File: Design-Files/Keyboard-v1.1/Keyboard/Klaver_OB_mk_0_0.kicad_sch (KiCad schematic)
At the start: 322 parts, among them J1 TYPE-C-31-M-13C, J3 Conn_01x04, J4 Conn_01x03, J5 TYPE-C-31-M-13C, J7 Conn_01x04, J8 Conn_01x03, Q1 BSS138, Q2 BSS138, U1 RP2040, U2 NCP1117LPST33T3G, U3 TPD4E05U06DQAR, U4 W25Q128JVSIQ, U5 TPD4E05U06DQAR, U6 W25Q128JVSIQ, U7 NCP1117LPST33T3G, U8 RP2040, Y1 12MHz 18pF, Y2 12MHz 18pF

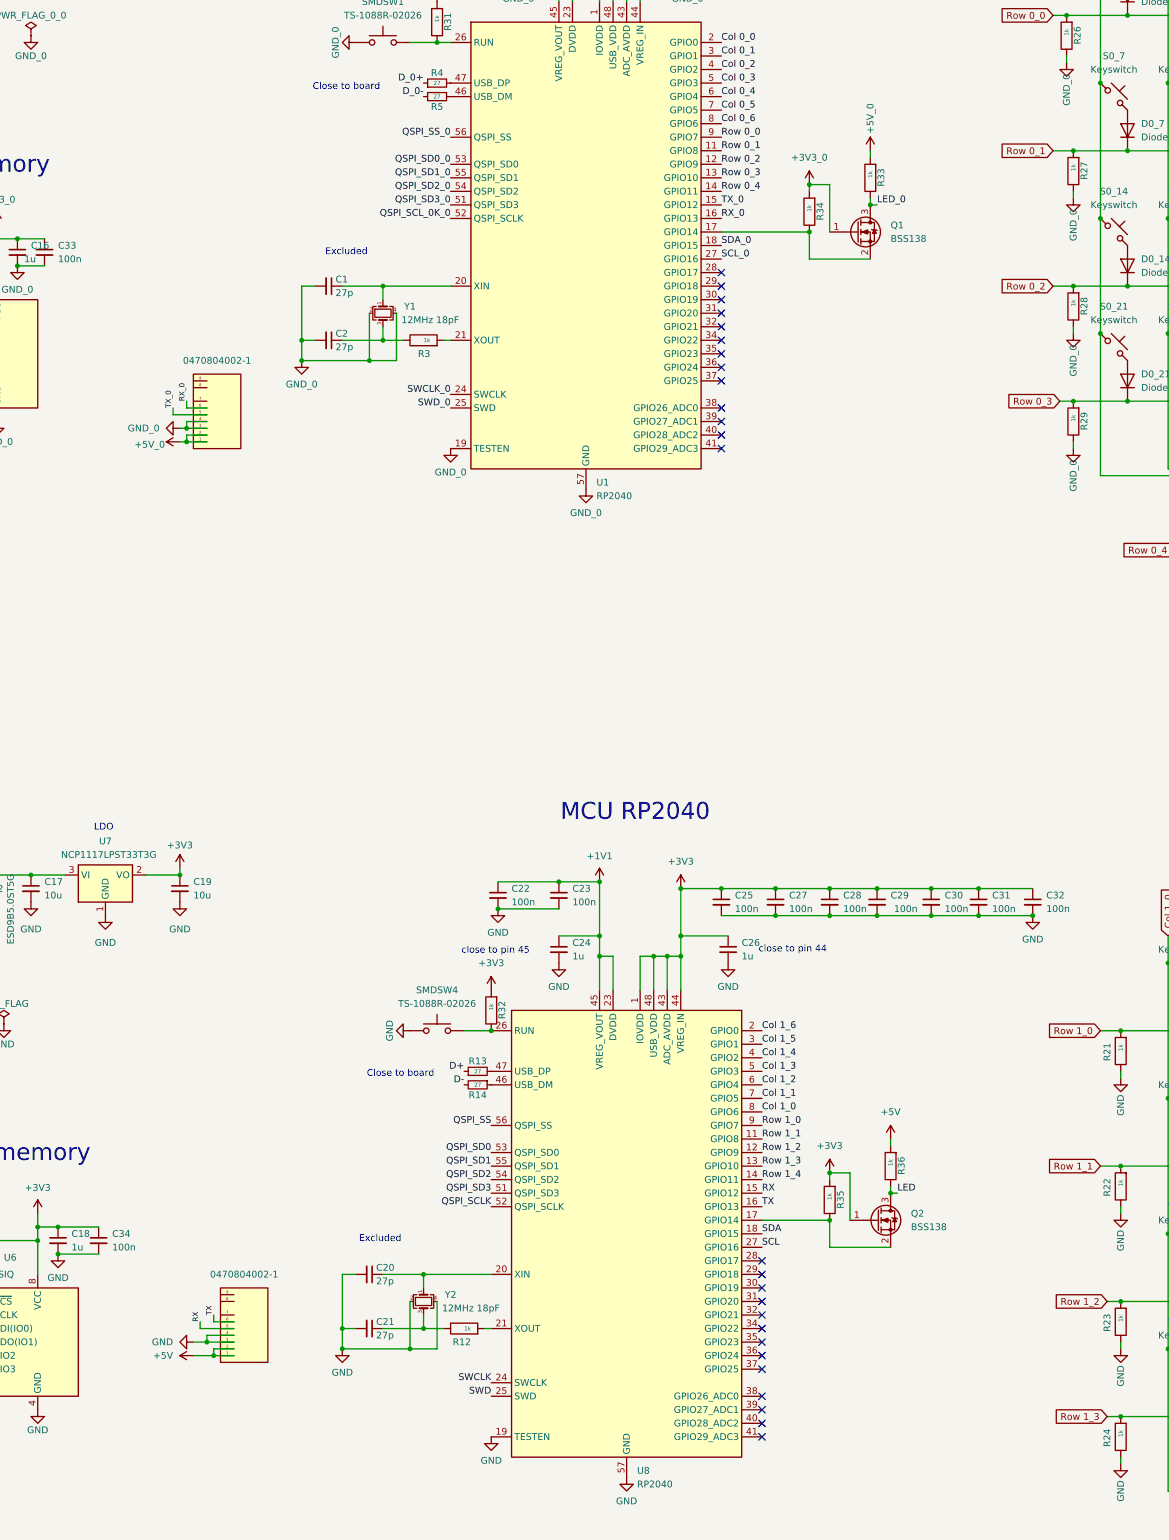
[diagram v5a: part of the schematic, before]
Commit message: #3  changed trrs connector and added zener diodes
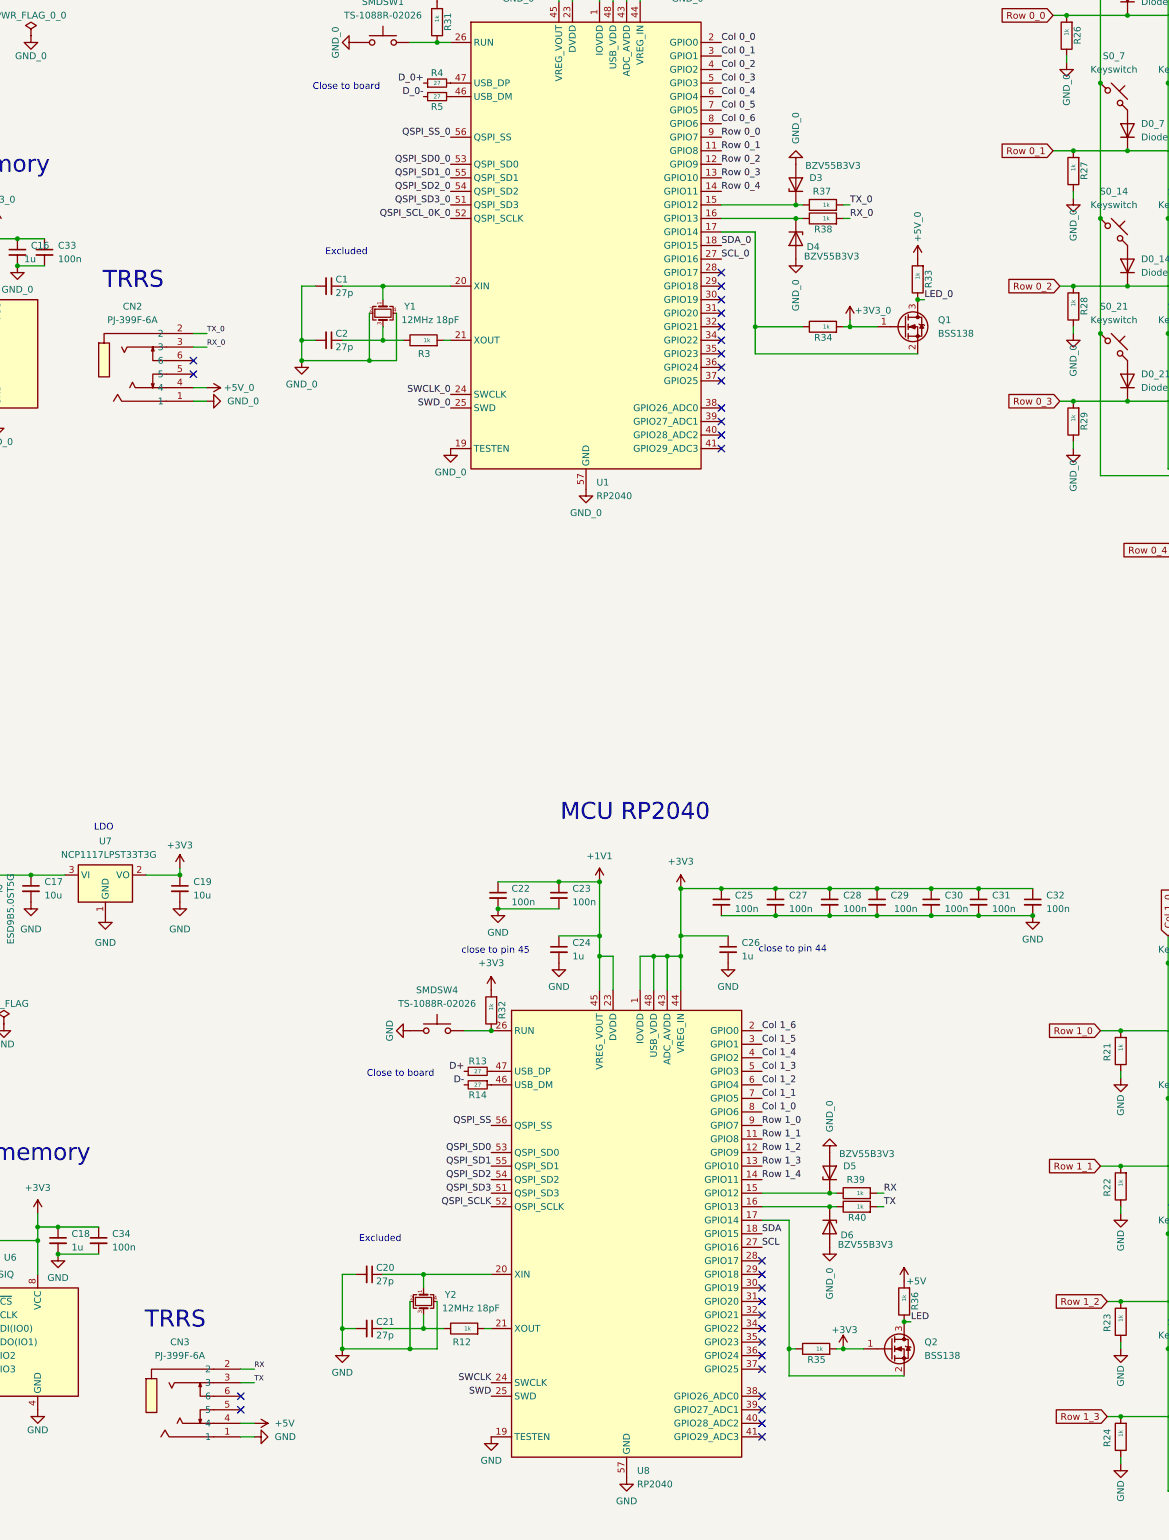
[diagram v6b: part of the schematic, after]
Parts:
- removed sata1, sata3: 0470804002-1, sata molex 2:sata molex1, symbol 5607-4200-SH:0470804002new
- added CN2, CN3: PJ-399F-6A, easyeda2kicad:AUDIO-SMD_PJ-399F-6A, symbol Library:PJ-399F-6A
- added D3, D4, D5, D6: BZV55B3V3, Diode_SMD:D_MiniMELF, symbol Diode:BZV55B3V3
- added R37, R38, R39, R40: 1k, Resistor_SMD:R_0402_1005Metric, symbol Library:R
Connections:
- net +5V: now also CN3.4
- net +5V_0: now also CN2.4
- net GND: now also CN3.1
- net GND_0: now also CN2.1, D3.2 (A), D4.2 (A), D5.2 (A), D6.2 (A)
- net RX: now also CN3.2, R39.2; no longer U8.15 (GPIO12)
- net RX_0: now also CN2.3, R38.2; no longer U1.16 (GPIO13)
- net TX: now also CN3.3, R40.2; no longer U8.16 (GPIO13)
- net TX_0: now also CN2.2, R37.2; no longer U1.15 (GPIO12)
- new net: D6.1 (K), R40.1, U8.16 (GPIO13)
- new net: D3.1 (K), R37.1, U1.15 (GPIO12)
- new net: D4.1 (K), R38.1, U1.16 (GPIO13)
- new net: D5.1 (K), R39.1, U8.15 (GPIO12)
- no-connect marks 32 -> 36
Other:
- note added: "TRRS"
- moved on the sheet: Q1, Q2, R33, R34, R35, R36

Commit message: #3 corrected TX RX
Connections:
- net RX: now also R40.2; no longer R39.2
- net TX: now also R39.2; no longer R40.2
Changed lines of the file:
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@@
 	(wire
 		(pts
+			(xy 273.05 281.94) (xy 274.32 281.94)
+		)
+		(stroke
+			(width 0)
+			(type default)
+		)
+	)
+	(wire
+		(pts
 			(xy 472.44 224.79) (xy 480.06 224.79)
 		)
@@
 	(wire
 		(pts
-			(xy 273.05 281.94) (xy 274.32 281.94)
-		)
-		(stroke
-			(width 0)
-			(type default)
-		)
-	)
-	(wire
-		(pts
 			(xy 201.93 226.06) (xy 213.36 226.06)
 		)
@@
 	(wire
 		(pts
-			(xy 273.05 279.4) (xy 274.32 279.4)
+			(xy 332.74 130.81) (xy 345.44 130.81)
 		)
 		(stroke
@@
 	(wire
 		(pts
-			(xy 332.74 130.81) (xy 345.44 130.81)
+			(xy 370.84 58.42) (xy 383.54 58.42)
 		)
 		(stroke
@@
 	(wire
 		(pts
-			(xy 370.84 58.42) (xy 383.54 58.42)
+			(xy 153.67 322.58) (xy 156.21 322.58)
 		)
 		(stroke
@@
 	(wire
 		(pts
-			(xy 153.67 322.58) (xy 156.21 322.58)
+			(xy 327.66 231.14) (xy 327.66 236.22)
 		)
 		(stroke
@@
 	(wire
 		(pts
-			(xy 327.66 231.14) (xy 327.66 236.22)
+			(xy 387.35 139.7) (xy 365.76 139.7)
 		)
 		(stroke
@@
 	(wire
 		(pts
-			(xy 387.35 139.7) (xy 365.76 139.7)
+			(xy 314.96 71.12) (xy 314.96 96.52)
 		)
 		(stroke
@@
 	(wire
 		(pts
-			(xy 314.96 71.12) (xy 314.96 96.52)
+			(xy 538.48 227.33) (xy 538.48 234.95)
 		)
 		(stroke
@@
 	(wire
 		(pts
-			(xy 538.48 227.33) (xy 538.48 234.95)
+			(xy 273.05 279.4) (xy 274.32 279.4)
 		)
 		(stroke
@@
 	)
 	(label "TX"
-		(at 274.32 281.94 0)
+		(at 274.32 279.4 0)
 		(fields_autoplaced yes)
 		(effects
@@
 	)
 	(label "RX"
-		(at 274.32 279.4 0)
+		(at 274.32 281.94 0)
 		(fields_autoplaced yes)
 		(effects
